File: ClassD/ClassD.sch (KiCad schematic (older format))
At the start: 54 parts, among them P1 RedRCA, P2 WhiteRCA, P3 CONN_01X02, P4 CONN_01X02, P5 CONN_01X02, SW1 SW_PUSH, SW2 SW_PUSH, U1 TDA7491LP, U2 MCP1700T

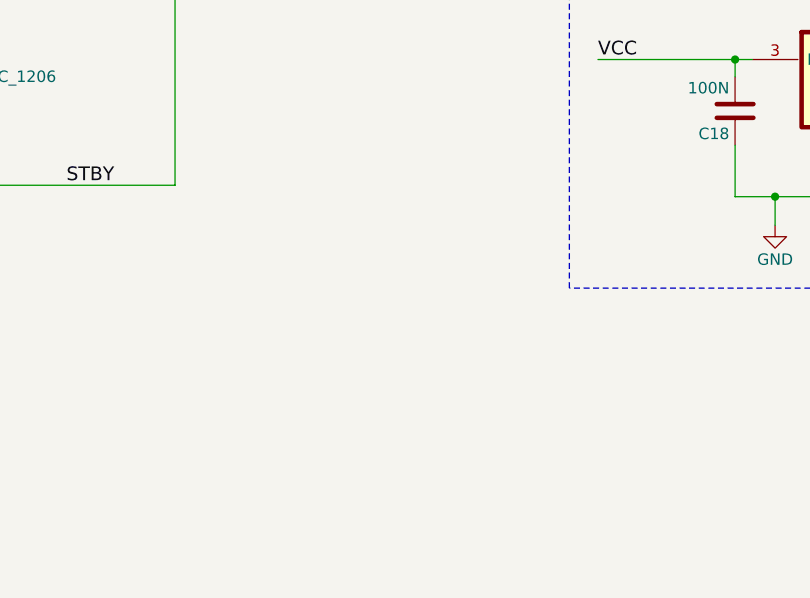
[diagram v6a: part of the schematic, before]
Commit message: Added ferrites, finished component grouping
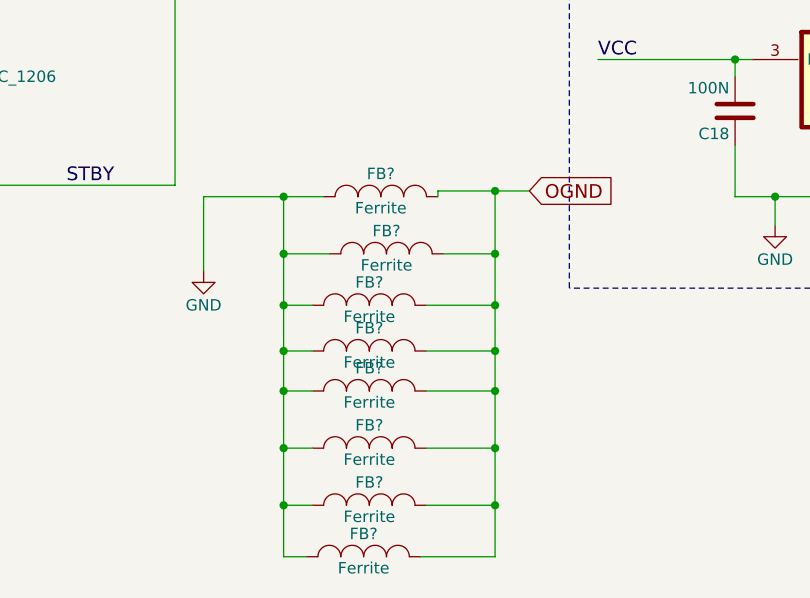
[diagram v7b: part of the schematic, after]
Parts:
- added FB? (x8): Ferrite, Resistors_SMD:R_0805, symbol INDUCTOR_SMALL
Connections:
- net GND: now also FB?.1, FB?.1, FB?.1, FB?.1, FB?.1, FB?.1, FB?.1, FB?.1, FB?.2, FB?.2, FB?.2, FB?.2, FB?.2, FB?.2, FB?.2, FB?.2
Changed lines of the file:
@@
 	8200 6250 8200 6050
 Connection ~ 8200 6050
+$Comp
+L INDUCTOR_SMALL FB?
+U 1 1 56CB8AF1
+P 5600 6050
+F 0 "FB?" H 5600 6150 50  0000 C CNN
+F 1 "Ferrite" H 5600 6000 50  0000 C CNN
+F 2 "Resistors_SMD:R_0805" H 5600 6050 50  0001 C CNN
+F 3 "" H 5600 6050 50  0000 C CNN
+	1    5600 6050
+	1    0    0    -1
+$EndComp
+$Comp
+L INDUCTOR_SMALL FB?
+U 1 1 56CB91F1
+P 5625 6300
+F 0 "FB?" H 5625 6400 50  0000 C CNN
+F 1 "Ferrite" H 5625 6250 50  0000 C CNN
+F 2 "Resistors_SMD:R_0805" H 5625 6300 50  0001 C CNN
+F 3 "" H 5625 6300 50  0000 C CNN
+	1    5625 6300
+	1    0    0    -1
+$EndComp
+$Comp
+L INDUCTOR_SMALL FB?
+U 1 1 56CB92D3
+P 5550 6525
+F 0 "FB?" H 5550 6625 50  0000 C CNN
+F 1 "Ferrite" H 5550 6475 50  0000 C CNN
+F 2 "Resistors_SMD:R_0805" H 5550 6525 50  0001 C CNN
+F 3 "" H 5550 6525 50  0000 C CNN
+	1    5550 6525
+	1    0    0    -1
+$EndComp
+$Comp
+L INDUCTOR_SMALL FB?
+U 1 1 56CB93A8
+P 5550 6725
+F 0 "FB?" H 5550 6825 50  0000 C CNN
+F 1 "Ferrite" H 5550 6675 50  0000 C CNN
+F 2 "Resistors_SMD:R_0805" H 5550 6725 50  0001 C CNN
+F 3 "" H 5550 6725 50  0000 C CNN
+	1    5550 6725
+	1    0    0    -1
+$EndComp
+$Comp
+L INDUCTOR_SMALL FB?
+U 1 1 56CB9472
+P 5550 6900
+F 0 "FB?" H 5550 7000 50  0000 C CNN
+F 1 "Ferrite" H 5550 6850 50  0000 C CNN
+F 2 "Resistors_SMD:R_0805" H 5550 6900 50  0001 C CNN
+F 3 "" H 5550 6900 50  0000 C CNN
+	1    5550 6900
+	1    0    0    -1
+$EndComp
+$Comp
+L INDUCTOR_SMALL FB?
+U 1 1 56CB953D
+P 5550 7150
+F 0 "FB?" H 5550 7250 50  0000 C CNN
+F 1 "Ferrite" H 5550 7100 50  0000 C CNN
+F 2 "Resistors_SMD:R_0805" H 5550 7150 50  0001 C CNN
+F 3 "" H 5550 7150 50  0000 C CNN
+	1    5550 7150
+	1    0    0    -1
+$EndComp
+$Comp
+L INDUCTOR_SMALL FB?
+U 1 1 56CB9611
+P 5550 7400
+F 0 "FB?" H 5550 7500 50  0000 C CNN
+F 1 "Ferrite" H 5550 7350 50  0000 C CNN
+F 2 "Resistors_SMD:R_0805" H 5550 7400 50  0001 C CNN
+F 3 "" H 5550 7400 50  0000 C CNN
+	1    5550 7400
+	1    0    0    -1
+$EndComp
+$Comp
+L INDUCTOR_SMALL FB?
+U 1 1 56CB96EA
+P 5525 7625
+F 0 "FB?" H 5525 7725 50  0000 C CNN
+F 1 "Ferrite" H 5525 7575 50  0000 C CNN
+F 2 "Resistors_SMD:R_0805" H 5525 7625 50  0001 C CNN
+F 3 "" H 5525 7625 50  0000 C CNN
+	1    5525 7625
+	1    0    0    -1
+$EndComp
+Wire Wire Line
+	4825 6050 5350 6050
+Wire Wire Line
+	4825 6050 4825 6375
+$Comp
+L GND #PWR?
+U 1 1 56CB9A78
+P 4825 6375
+F 0 "#PWR?" H 4825 6125 50  0001 C CNN
+F 1 "GND" H 4825 6225 50  0000 C CNN
+F 2 "" H 4825 6375 50  0000 C CNN
+F 3 "" H 4825 6375 50  0000 C CNN
+	1    4825 6375
+	1    0    0    -1
+$EndComp
+Text GLabel 6250 6025 2    60   Input ~ 0
+OGND
+Wire Wire Line
+	6250 6025 5850 6025
+Wire Wire Line
+	5850 6025 5850 6050
+Wire Wire Line
+	5875 6300 6100 6300
+Wire Wire Line
+	6100 6025 6100 7625
+Connection ~ 6100 6025
+Wire Wire Line
+	6100 6525 5800 6525
+Connection ~ 6100 6300
+Wire Wire Line
+	6100 6725 5800 6725
+Connection ~ 6100 6525
+Wire Wire Line
+	6100 6900 5800 6900
+Connection ~ 6100 6725
+Wire Wire Line
+	6100 7150 5800 7150
+Connection ~ 6100 6900
+Wire Wire Line
+	6100 7400 5800 7400
+Connection ~ 6100 7150
+Wire Wire Line
+	6100 7625 5775 7625
+Connection ~ 6100 7400
+Wire Wire Line
+	5375 6300 5175 6300
+Wire Wire Line
+	5175 6050 5175 7625
+Connection ~ 5175 6050
+Wire Wire Line
+	5175 6525 5300 6525
+Connection ~ 5175 6300
+Wire Wire Line
+	5175 6725 5300 6725
+Connection ~ 5175 6525
+Wire Wire Line
+	5175 6900 5300 6900
+Connection ~ 5175 6725
+Wire Wire Line
+	5175 7150 5300 7150
+Connection ~ 5175 6900
+Wire Wire Line
+	5175 7400 5300 7400
+Connection ~ 5175 7150
+Wire Wire Line
+	5175 7625 5275 7625
+Connection ~ 5175 7400
 $EndSCHEMATC

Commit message: Added ferrites, finished component grouping
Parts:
- gave numbers to parts that had none: 8
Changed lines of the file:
@@
 Connection ~ 8200 6050
 $Comp
-L INDUCTOR_SMALL FB?
+L INDUCTOR_SMALL FB7
 U 1 1 56CB8AF1
 P 5600 6050
-F 0 "FB?" H 5600 6150 50  0000 C CNN
+F 0 "FB7" H 5600 6150 50  0000 C CNN
 F 1 "Ferrite" H 5600 6000 50  0000 C CNN
 F 2 "Resistors_SMD:R_0805" H 5600 6050 50  0001 C CNN
@@
 $EndComp
 $Comp
-L INDUCTOR_SMALL FB?
+L INDUCTOR_SMALL FB8
 U 1 1 56CB91F1
 P 5625 6300
-F 0 "FB?" H 5625 6400 50  0000 C CNN
+F 0 "FB8" H 5625 6400 50  0000 C CNN
 F 1 "Ferrite" H 5625 6250 50  0000 C CNN
 F 2 "Resistors_SMD:R_0805" H 5625 6300 50  0001 C CNN
@@
 $EndComp
 $Comp
-L INDUCTOR_SMALL FB?
+L INDUCTOR_SMALL FB2
 U 1 1 56CB92D3
 P 5550 6525
-F 0 "FB?" H 5550 6625 50  0000 C CNN
+F 0 "FB2" H 5550 6625 50  0000 C CNN
 F 1 "Ferrite" H 5550 6475 50  0000 C CNN
 F 2 "Resistors_SMD:R_0805" H 5550 6525 50  0001 C CNN
@@
 $EndComp
 $Comp
-L INDUCTOR_SMALL FB?
+L INDUCTOR_SMALL FB3
 U 1 1 56CB93A8
 P 5550 6725
-F 0 "FB?" H 5550 6825 50  0000 C CNN
+F 0 "FB3" H 5550 6825 50  0000 C CNN
 F 1 "Ferrite" H 5550 6675 50  0000 C CNN
 F 2 "Resistors_SMD:R_0805" H 5550 6725 50  0001 C CNN
@@
 $EndComp
 $Comp
-L INDUCTOR_SMALL FB?
+L INDUCTOR_SMALL FB4
 U 1 1 56CB9472
 P 5550 6900
-F 0 "FB?" H 5550 7000 50  0000 C CNN
+F 0 "FB4" H 5550 7000 50  0000 C CNN
 F 1 "Ferrite" H 5550 6850 50  0000 C CNN
 F 2 "Resistors_SMD:R_0805" H 5550 6900 50  0001 C CNN
@@
 $EndComp
 $Comp
-L INDUCTOR_SMALL FB?
+L INDUCTOR_SMALL FB5
 U 1 1 56CB953D
 P 5550 7150
-F 0 "FB?" H 5550 7250 50  0000 C CNN
+F 0 "FB5" H 5550 7250 50  0000 C CNN
 F 1 "Ferrite" H 5550 7100 50  0000 C CNN
 F 2 "Resistors_SMD:R_0805" H 5550 7150 50  0001 C CNN
@@
 $EndComp
 $Comp
-L INDUCTOR_SMALL FB?
+L INDUCTOR_SMALL FB6
 U 1 1 56CB9611
 P 5550 7400
-F 0 "FB?" H 5550 7500 50  0000 C CNN
+F 0 "FB6" H 5550 7500 50  0000 C CNN
 F 1 "Ferrite" H 5550 7350 50  0000 C CNN
 F 2 "Resistors_SMD:R_0805" H 5550 7400 50  0001 C CNN
@@
 $EndComp
 $Comp
-L INDUCTOR_SMALL FB?
+L INDUCTOR_SMALL FB1
 U 1 1 56CB96EA
 P 5525 7625
-F 0 "FB?" H 5525 7725 50  0000 C CNN
+F 0 "FB1" H 5525 7725 50  0000 C CNN
 F 1 "Ferrite" H 5525 7575 50  0000 C CNN
 F 2 "Resistors_SMD:R_0805" H 5525 7625 50  0001 C CNN
@@
 	4825 6050 4825 6375
 $Comp
-L GND #PWR?
+L GND #PWR012
 U 1 1 56CB9A78
 P 4825 6375
-F 0 "#PWR?" H 4825 6125 50  0001 C CNN
+F 0 "#PWR012" H 4825 6125 50  0001 C CNN
 F 1 "GND" H 4825 6225 50  0000 C CNN
 F 2 "" H 4825 6375 50  0000 C CNN
